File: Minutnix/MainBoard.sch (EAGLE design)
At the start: 128 parts, among them IC1 MEGA8-AI, IC10 TPIC6C596PW, IC11 TPIC6C596PW, IC12 TPIC6C596PW, IC13 TPIC6C596PW, IC2 TPIC6C596PW, IC3 TPIC6C596PW, IC4 TPIC6C596PW, IC5 TPIC6C596PW, IC6 TP4056, IC8 FT230XS, IC9 SC4503, Q1 32.768kHz, T1 DMN3024LSD

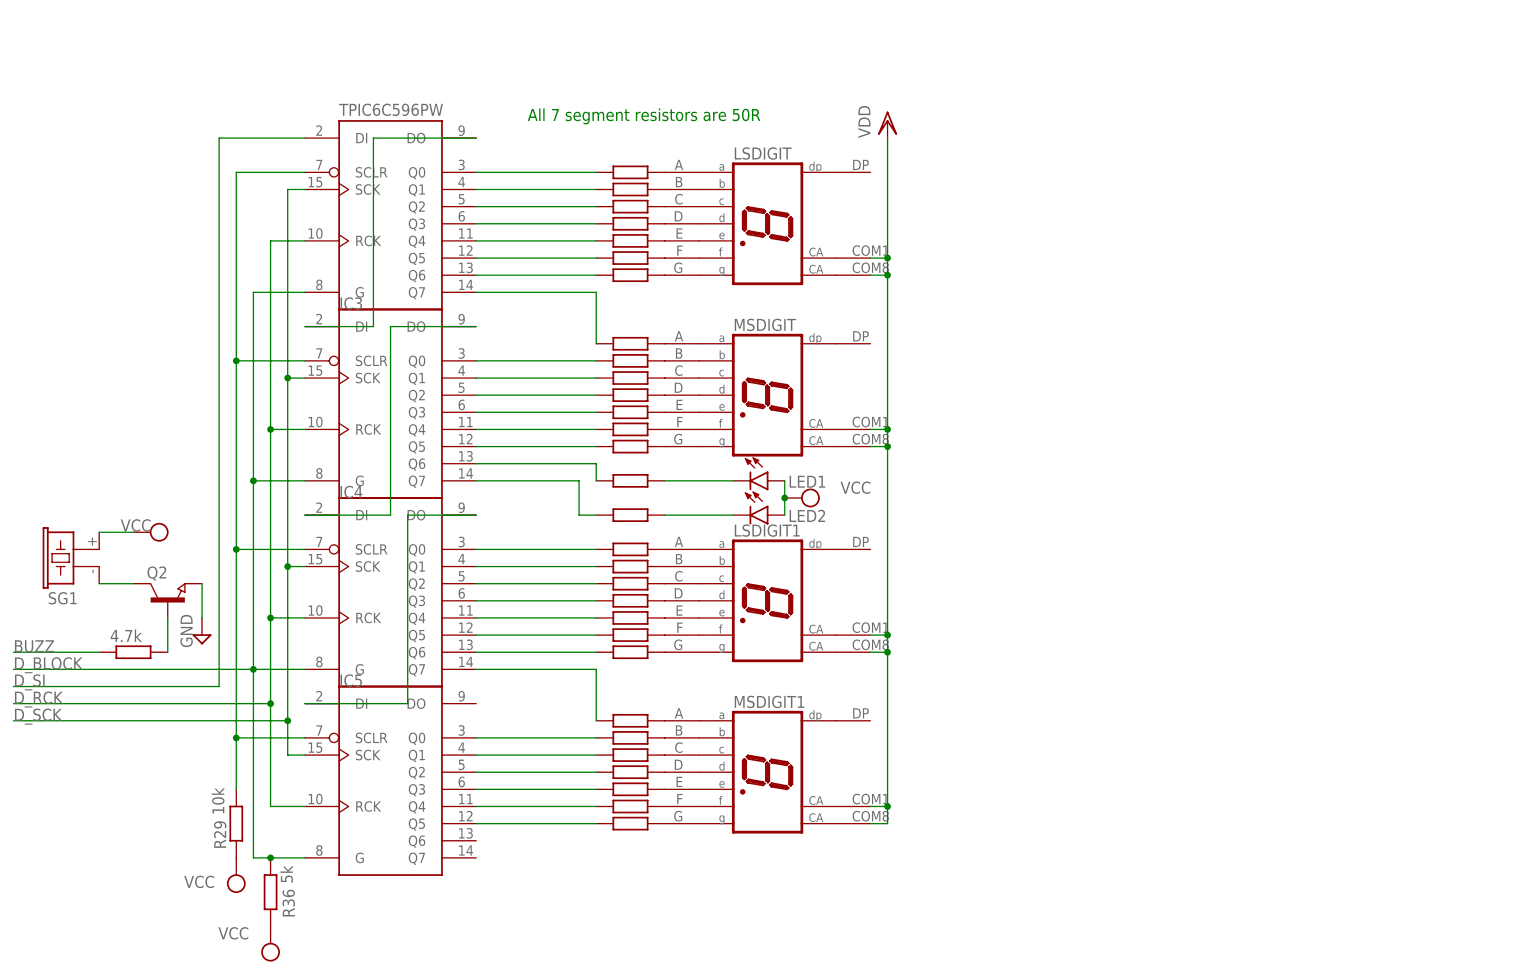
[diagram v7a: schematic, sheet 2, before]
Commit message: Vreg done, formatting
TODO:
solve offgrid
check charger circuit if proper
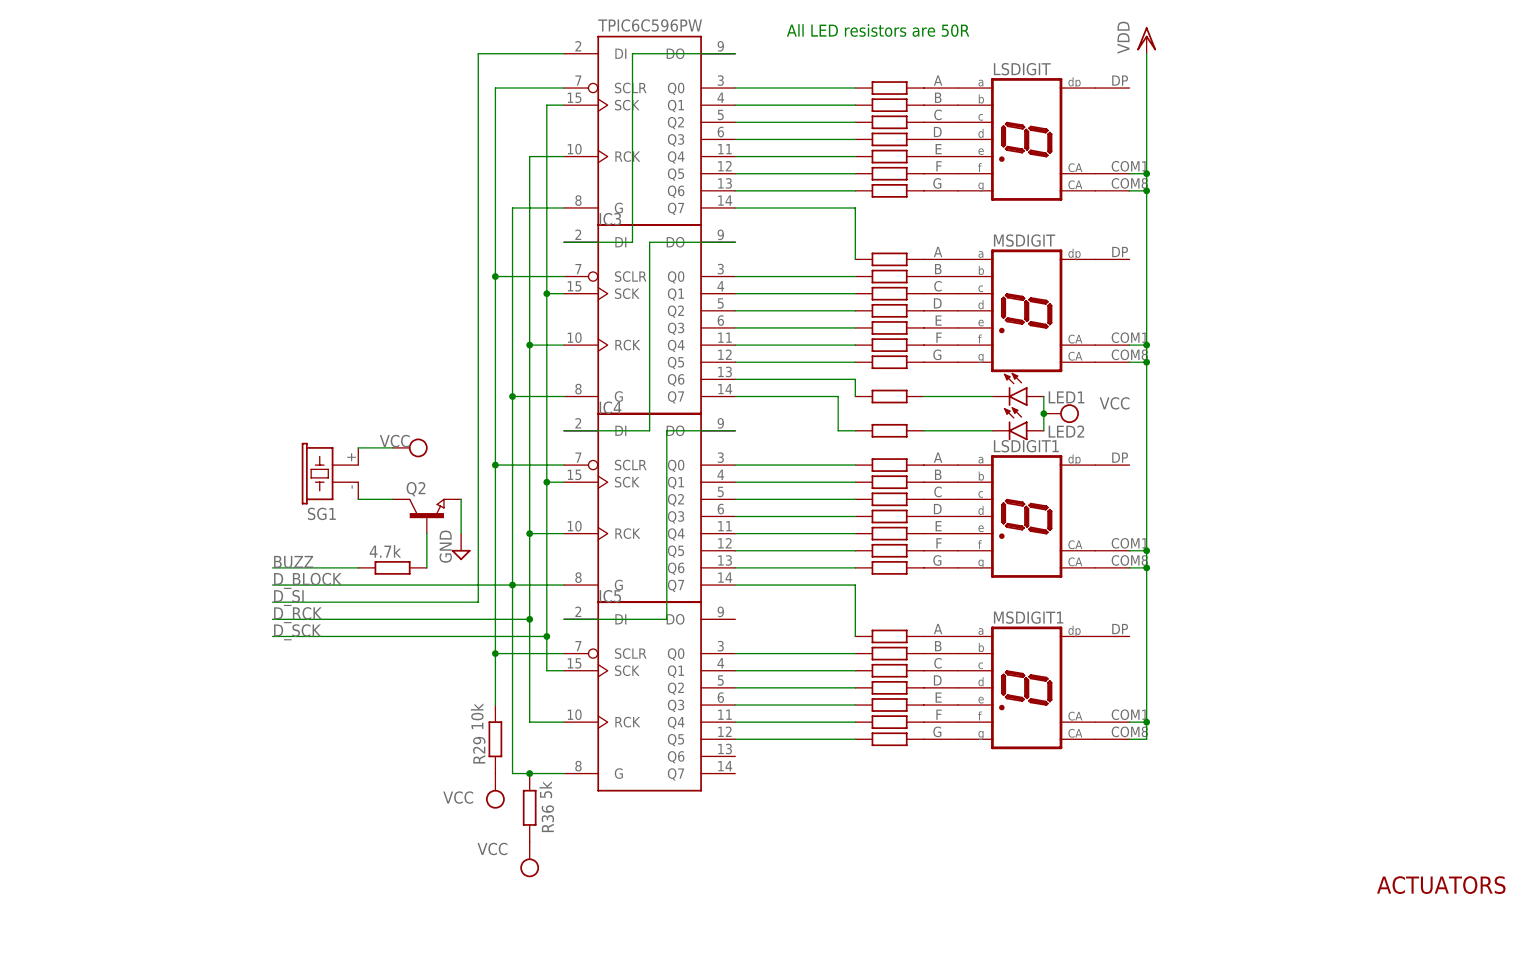
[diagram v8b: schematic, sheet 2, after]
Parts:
- removed C1, C2: 22pF, capacitor-wima:C2.5/2
- removed C10: 100nF, rcl:CPOL-EU140CLH-1010
- removed C3: 470uF, rcl:CPOL-EU140CLH-1010
- removed C4: 100uF, rcl:CPOL-EU140CLH-1010
- removed Q1: 32.768kHz, crystal:CRYSTALTC26V
- removed R0, R33: 4.7k, rcl:R-EU_R1206
- removed R32: 7.05k, rcl:R-EU_R1206
- removed SHOTTKYDIODE: S2A, s2x_10:S2A
- added ATMEGA328P: ATMEGA328P-AU, atmega328:ATMEGA328P-AU
- added C29, C30: 22pF, capacitor-wima:C2.5/2
- added C31: 470uF, rcl:CPOL-EU140CLH-1010
- added C32: 100uF, rcl:CPOL-EU140CLH-1010
- added C33: 100nF, rcl:CPOL-EU140CLH-1010
- added L5: BLM15HB121SN1, inductors:BLM15HB121SN1
- added Q4: 32.768kHz, crystal:CRYSTALTC26V
- added R56, R58: 4.7k, rcl:R-EU_R1206
- added R57: 7.05k, rcl:R-EU_R1206
- added S1: (no value), switch:MS243
- added SHOTTKYDIODE3: S2A, s2x_10:S2A
- C24: value 0.1u -> 10pF
- C25: value 0.1u -> 10 - 22uF
- C26: value 0.1u -> 56nF
- C27: value 0.1u -> 4.7u
- L3: value MS42 -> 4.237H
- R53: value 50 -> 15k4
- R54: value 50 -> 620k
- R55: value 50 -> 100k
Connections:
- removed net N$12: C10.+, IC1.AREF, R32.1, R33.2
- removed net N$2: C2.2, IC1.PB7(XTAL2/TOSC2), Q1.1
- removed net N$22: IC1.PC6(/RESET), R0.1
- removed net N$35: C3.+, IC1.PD7(AIN1), IC1.VCC@1, IC1.VCC@2, SHOTTKYDIODE.C
- removed net N$4: C4.+, IC1.AVCC
- new net AREF: ATMEGA328P.AREF, C33.+, IC1.AREF, R57.1, R58.2
- new net AVCC: ATMEGA328P.AVCC, C32.+, IC1.AVCC, L5.2
- new net RESET: ATMEGA328P.PC6, IC1.PC6(/RESET), R56.1
- new net S_VCC: ATMEGA328P.PD7, ATMEGA328P.VCC, ATMEGA328P.VCC_2, C31.+, IC1.PD7(AIN1), IC1.VCC@1, IC1.VCC@2, L5.1, SHOTTKYDIODE3.C
- new net XTAL1: ATMEGA328P.PB6, C29.2, IC1.PB6(XTAL1/TOSC1), Q4.2
- new net XTAL2: ATMEGA328P.PB7, C30.2, IC1.PB7(XTAL2/TOSC2), Q4.1
- net BUZZ: now also ATMEGA328P.PD5
- net D_BLOCK: now also ATMEGA328P.PB2
- net D_RCK: now also ATMEGA328P.PB1, IC1.PD5(T1); no longer IC1.PB4(MISO)
- net D_SCK: now also ATMEGA328P.PB5
- net D_SI: now also ATMEGA328P.PB3
- net EXP_INT: now also ATMEGA328P.PD2
- net EXP_SCL: now also ATMEGA328P.PC5
- net EXP_SDA: now also ATMEGA328P.PC4
- net GND: now also ATMEGA328P.GND, ATMEGA328P.GND_2, ATMEGA328P.GND_3, C29.1, C30.1, C31.-, C32.-, C33.-, R57.2; no longer C1.1, C10.-, C2.1, C3.-, C4.-, R32.2
- net L1: now also ATMEGA328P.PD4, IC1.PD4(XCK/T0); no longer IC1.PB0(ICP)
- net L2: now also ATMEGA328P.PD3, IC1.PD3(INT1); no longer IC1.PD5(T1)
- net L3: now also ATMEGA328P.PC3
- net L4: now also ATMEGA328P.PC2
- net L5: now also ATMEGA328P.PC1
- net L6: now also ATMEGA328P.PC0
- net LIGHT_SENS: now also ATMEGA328P.ADC6
- net N$1: now also C11.2, G1.+, IC6.BAT, R40.1, S1.P; no longer C1.2, IC1.PB6(XTAL1/TOSC1), Q1.2
- net RXD: now also ATMEGA328P.PD0
- net TXD: now also ATMEGA328P.PD1
- net VCC: now also ATMEGA328P.PD6, R56.2, R58.1, S1.S, SHOTTKYDIODE3.A; no longer C11.2, G1.+, IC6.BAT, R0.2, R33.1, R40.1, SHOTTKYDIODE.A
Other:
- note added: "3.04<L<5.2"
- note added: "ACTUATORS"
- note added: "AREF"
- note added: "AVCC Supply"
- note added: "All LED resistors are 50R"
- note added: "Atmega328p version"
- note added: "Atmega8 version"
- note added: "BATTERY CHARGER AND PROTECTION"
- note added: "CLOCK QUARTZ"
- note added: "CONTROL"
- note added: "DISPLAY SUPPLY PORTS"
- note added: "FTDI USB - UART INTERFACE"
- note added: "ID musi wytrzymać prąd obciążenia (0.6A)"
- note added: "INPUTS"
- note added: "INTERFACE MAINBOARD - CONTROLS"
- note added: "LIGHT SENSOR"
- note added: "MICRO USB INPUT"
- note added: "R54 i R55 muszą być w tej proporcji, tolerancja 1%"
- note added: "RESET"
- note added: "SUPPLY"
- note added: "VCC Logic supply"
- note added: "VDD BOOST VREG"
- note removed: "All 7 segment resistors are 50R"
- moved on the sheet: B_GND, B_VCC, C11, C13, C19, C20, C24, C25, C26, C27, C5, C6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
